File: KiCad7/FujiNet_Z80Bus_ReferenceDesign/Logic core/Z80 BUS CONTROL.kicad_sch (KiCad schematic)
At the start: 9 parts, among them IC6 7432N, IC7 7432N

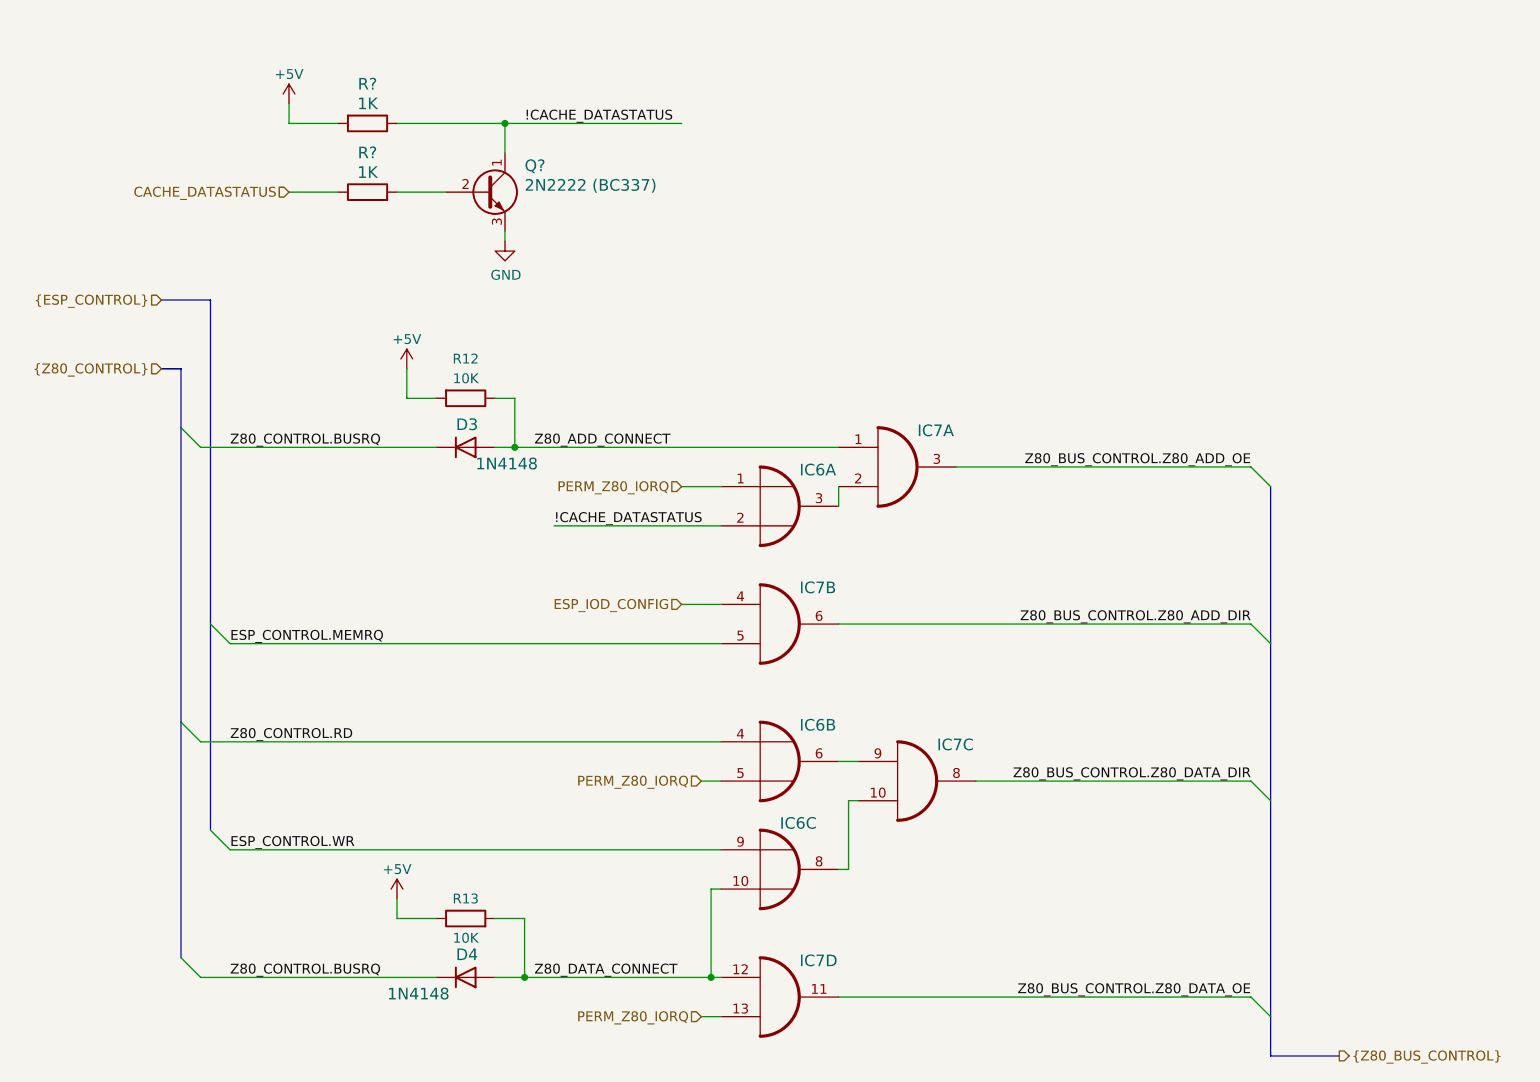
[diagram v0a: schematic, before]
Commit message: Unpicked CoreLogic Buses, some symbol updates
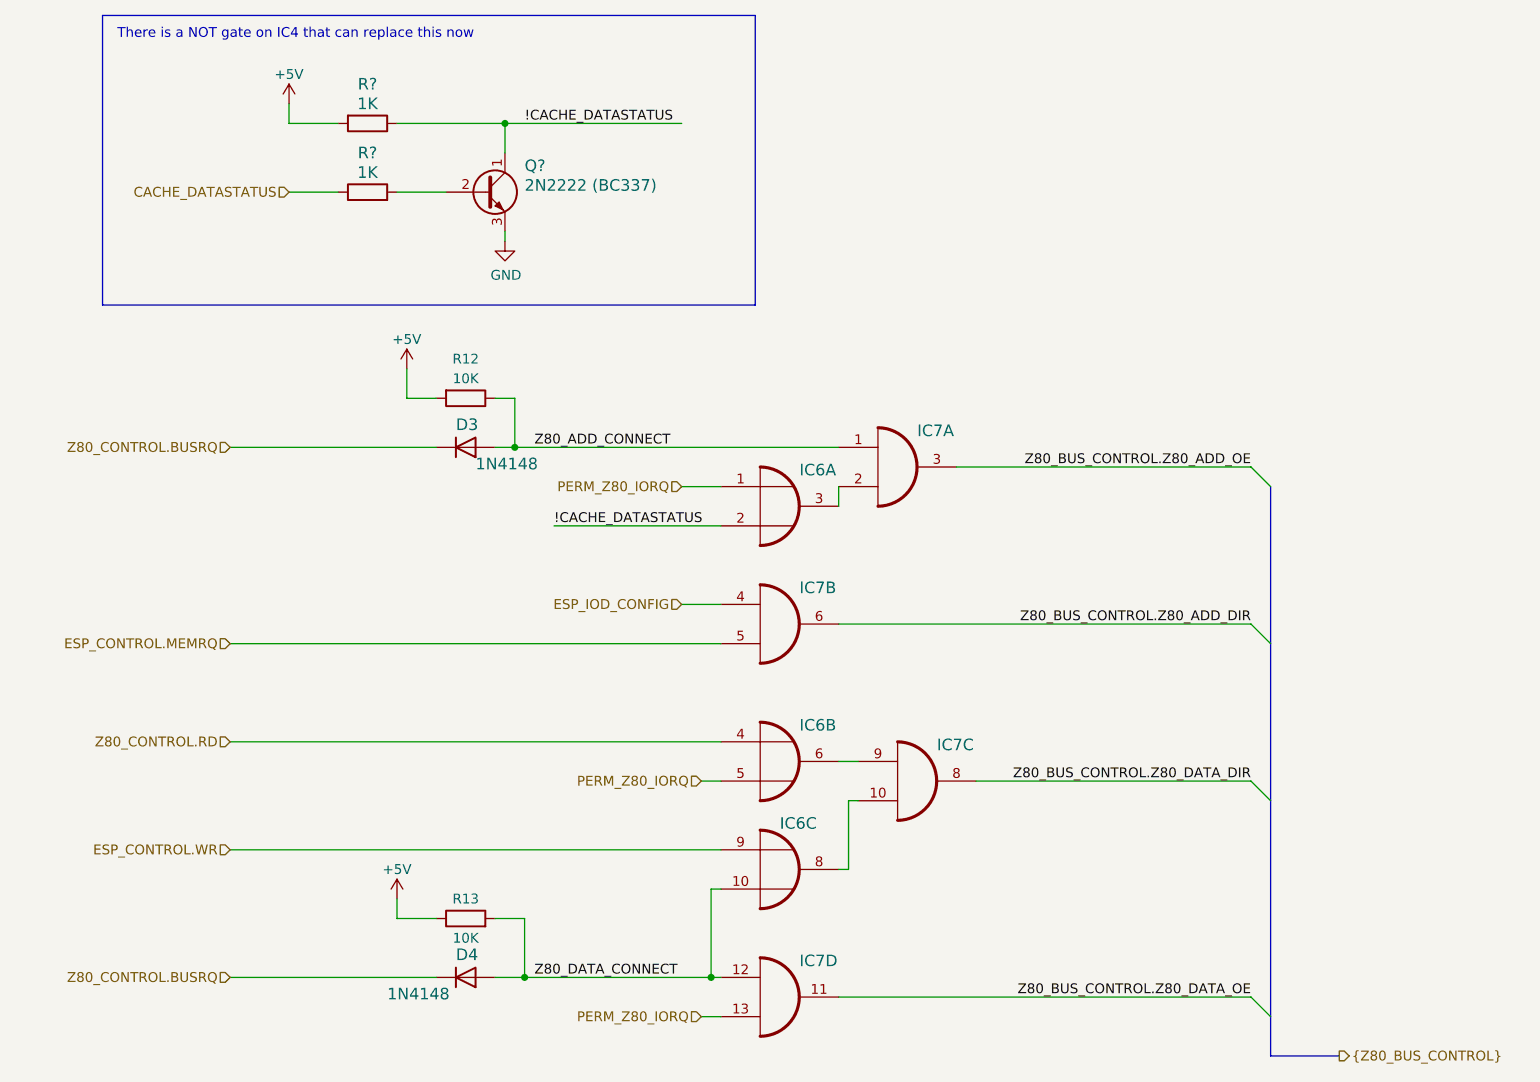
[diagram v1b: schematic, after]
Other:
- note added: "There is a NOT gate on IC4 that can replace this now"
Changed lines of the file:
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@@
-    (stroke (width 0) (type default))
-  )
-  (bus_entry (at 53.34 97.79) (size 2.54 2.54)
-    (stroke (width 0) (type default))
-  )
-  (bus_entry (at 49.53 140.97) (size 2.54 2.54)
     (stroke (width 0) (type default))
   )
@@
     (stroke (width 0) (type default))
   )
-  (bus_entry (at 52.07 74.93) (size -2.54 -2.54)
-    (stroke (width 0) (type default))
-  )
-  (bus_entry (at 49.53 110.49) (size 2.54 2.54)
-    (stroke (width 0) (type default))
-  )
-  (bus_entry (at 53.34 124.46) (size 2.54 2.54)
-    (stroke (width 0) (type default))
-  )
   (wire (pts (xy 91.44 33.02) (xy 91.44 36.83))
     (stroke (width 0) (type default))
@@
     (stroke (width 0) (type default))
   )
-  (bus (pts (xy 49.53 72.39) (xy 49.53 110.49))
-    (stroke (width 0) (type default))
-  )
   (wire (pts (xy 63.5 30.48) (xy 63.5 33.02))
     (stroke (width 0) (type default))
   )
-  (bus (pts (xy 46.99 64.77) (xy 49.53 64.77))
-    (stroke (width 0) (type default))
-  )
   (wire (pts (xy 119.38 80.01) (xy 114.3 80.01))
     (stroke (width 0) (type default))
@@
     (stroke (width 0) (type default))
   )
-  (bus (pts (xy 53.34 97.79) (xy 53.34 124.46))
-    (stroke (width 0) (type default))
-  )
   (wire (pts (xy 118.11 143.51) (xy 119.38 143.51))
     (stroke (width 0) (type default))
@@
     (stroke (width 0) (type default))
   )
-  (bus (pts (xy 46.99 55.88) (xy 53.34 55.88))
-    (stroke (width 0) (type default))
-  )
   (wire (pts (xy 63.5 33.02) (xy 69.85 33.02))
     (stroke (width 0) (type default))
@@
     (stroke (width 0) (type default))
   )
-  (wire (pts (xy 52.07 143.51) (xy 82.55 143.51))
-    (stroke (width 0) (type default))
-  )
   (wire (pts (xy 92.71 74.93) (xy 134.62 74.93))
     (stroke (width 0) (type default))
@@
     (stroke (width 0) (type default))
   )
-  (bus (pts (xy 49.53 110.49) (xy 49.53 140.97))
-    (stroke (width 0) (type default))
-  )
   (wire (pts (xy 118.11 132.08) (xy 119.38 132.08))
     (stroke (width 0) (type default))
@@
     (stroke (width 0) (type default))
   )
+  (wire (pts (xy 55.88 143.51) (xy 82.55 143.51))
+    (stroke (width 0) (type default))
+  )
   (wire (pts (xy 92.71 68.58) (xy 90.17 68.58))
     (stroke (width 0) (type default))
@@
     (stroke (width 0) (type default))
   )
-  (bus (pts (xy 49.53 64.77) (xy 49.53 72.39))
-    (stroke (width 0) (type default))
-  )
   (wire (pts (xy 116.84 118.11) (xy 119.38 118.11))
     (stroke (width 0) (type default))
@@
     (stroke (width 0) (type default))
   )
-  (bus (pts (xy 53.34 55.88) (xy 53.34 97.79))
-    (stroke (width 0) (type default))
-  )
-  (wire (pts (xy 52.07 113.03) (xy 119.38 113.03))
+  (wire (pts (xy 55.88 113.03) (xy 119.38 113.03))
     (stroke (width 0) (type default))
   )
@@
     (stroke (width 0) (type default))
   )
-  (wire (pts (xy 52.07 74.93) (xy 82.55 74.93))
+  (wire (pts (xy 55.88 74.93) (xy 82.55 74.93))
     (stroke (width 0) (type default))
   )
@@
     (stroke (width 0) (type default))
   )
-  (label "ESP_CONTROL.MEMRQ" (at 55.88 100.33 0) (fields_autoplaced)
+  (rectangle (start 39.37 19.05) (end 123.825 56.515)
+    (stroke (width 0) (type default))
+    (fill (type none))
+  )
+  (text "There is a NOT gate on IC4 that can replace this now"
+    (at 41.275 22.225 0)
     (effects (font (size 1.27 1.27)) (justify left bottom))
   )
@@
     (effects (font (size 1.27 1.27)) (justify right bottom))
   )
-  (label "Z80_CONTROL.RD" (at 55.88 113.03 0) (fields_autoplaced)
-    (effects (font (size 1.27 1.27)) (justify left bottom))
-  )
   (label "!CACHE_DATASTATUS" (at 93.98 33.02 0) (fields_autoplaced)
     (effects (font (size 1.27 1.27)) (justify left bottom))
@@
     (effects (font (size 1.27 1.27)) (justify left bottom))
   )
-  (label "Z80_CONTROL.BUSRQ" (at 55.88 143.51 0) (fields_autoplaced)
-    (effects (font (size 1.27 1.27)) (justify left bottom))
-  )
   (label "Z80_BUS_CONTROL.Z80_ADD_OE" (at 187.96 77.47 180) (fields_autoplaced)
     (effects (font (size 1.27 1.27)) (justify right bottom))
@@
     (effects (font (size 1.27 1.27)) (justify left bottom))
   )
-  (label "ESP_CONTROL.WR" (at 55.88 127 0) (fields_autoplaced)
-    (effects (font (size 1.27 1.27)) (justify left bottom))
-  )
-  (label "Z80_CONTROL.BUSRQ" (at 55.88 74.93 0) (fields_autoplaced)
-    (effects (font (size 1.27 1.27)) (justify left bottom))
-  )
   (hierarchical_label "PERM_Z80_IORQ" (shape input) (at 116.84 118.11 180) (fields_autoplaced)
     (effects (font (size 1.27 1.27)) (justify right))
@@
     (effects (font (size 1.27 1.27)) (justify right))
   )
-  (hierarchical_label "{ESP_CONTROL}" (shape input) (at 46.99 55.88 180) (fields_autoplaced)
+  (hierarchical_label "Z80_CONTROL.BUSRQ" (shape input) (at 55.88 74.93 180) (fields_autoplaced)
     (effects (font (size 1.27 1.27)) (justify right))
   )
@@
     (effects (font (size 1.27 1.27)) (justify left))
   )
+  (hierarchical_label "ESP_CONTROL.MEMRQ" (shape input) (at 55.88 100.33 180) (fields_autoplaced)
+    (effects (font (size 1.27 1.27)) (justify right))
+  )
   (hierarchical_label "PERM_Z80_IORQ" (shape input) (at 116.84 148.59 180) (fields_autoplaced)
     (effects (font (size 1.27 1.27)) (justify right))
   )
+  (hierarchical_label "Z80_CONTROL.BUSRQ" (shape input) (at 55.88 143.51 180) (fields_autoplaced)
+    (effects (font (size 1.27 1.27)) (justify right))
+  )
+  (hierarchical_label "Z80_CONTROL.RD" (shape input) (at 55.88 113.03 180) (fields_autoplaced)
+    (effects (font (size 1.27 1.27)) (justify right))
+  )
   (hierarchical_label "ESP_IOD_CONFIG" (shape input) (at 114.3 95.25 180) (fields_autoplaced)
     (effects (font (size 1.27 1.27)) (justify right))
@@
     (effects (font (size 1.27 1.27)) (justify right))
   )
-  (hierarchical_label "{Z80_CONTROL}" (shape input) (at 46.99 64.77 180) (fields_autoplaced)
+  (hierarchical_label "ESP_CONTROL.WR" (shape input) (at 55.88 127 180) (fields_autoplaced)
     (effects (font (size 1.27 1.27)) (justify right))
   )
@@
         )
         (path "/532c0392-800e-45cc-8170-6d32f2390e83/6a1fd481-1635-4a64-b244-c204161ad407/6bcd45ec-1810-4278-8058-96e26ec9b5f3"
-          (reference "IC6") (unit 3)
+          (reference "IC12") (unit 3)
         )
       )
@@
         )
         (path "/532c0392-800e-45cc-8170-6d32f2390e83/6a1fd481-1635-4a64-b244-c204161ad407/6bcd45ec-1810-4278-8058-96e26ec9b5f3"
-          (reference "#PWR027") (unit 1)
+          (reference "#PWR033") (unit 1)
         )
       )
@@
         )
         (path "/532c0392-800e-45cc-8170-6d32f2390e83/6a1fd481-1635-4a64-b244-c204161ad407/6bcd45ec-1810-4278-8058-96e26ec9b5f3"
-          (reference "IC6") (unit 2)
+          (reference "IC9") (unit 2)
         )
       )
@@
         )
         (path "/532c0392-800e-45cc-8170-6d32f2390e83/6a1fd481-1635-4a64-b244-c204161ad407/6bcd45ec-1810-4278-8058-96e26ec9b5f3"
-          (reference "IC6") (unit 1)
+          (reference "IC9") (unit 1)
         )
       )
@@
         )
         (path "/532c0392-800e-45cc-8170-6d32f2390e83/6a1fd481-1635-4a64-b244-c204161ad407/6bcd45ec-1810-4278-8058-96e26ec9b5f3"
-          (reference "D3") (unit 1)
+          (reference "D15") (unit 1)
         )
       )
@@
         )
         (path "/532c0392-800e-45cc-8170-6d32f2390e83/6a1fd481-1635-4a64-b244-c204161ad407/6bcd45ec-1810-4278-8058-96e26ec9b5f3"
-          (reference "IC7") (unit 4)
+          (reference "IC11") (unit 4)
         )
       )
@@
         )
         (path "/532c0392-800e-45cc-8170-6d32f2390e83/6a1fd481-1635-4a64-b244-c204161ad407/6bcd45ec-1810-4278-8058-96e26ec9b5f3"
-          (reference "R9") (unit 1)
+          (reference "R11") (unit 1)
         )
       )
@@
         )
         (path "/532c0392-800e-45cc-8170-6d32f2390e83/6a1fd481-1635-4a64-b244-c204161ad407/6bcd45ec-1810-4278-8058-96e26ec9b5f3"
-          (reference "R8") (unit 1)
+          (reference "R14") (unit 1)
         )
       )
@@
         )
         (path "/532c0392-800e-45cc-8170-6d32f2390e83/6a1fd481-1635-4a64-b244-c204161ad407/6bcd45ec-1810-4278-8058-96e26ec9b5f3"
-          (reference "IC7") (unit 3)
+          (reference "IC11") (unit 3)
         )
       )
@@
         )
         (path "/532c0392-800e-45cc-8170-6d32f2390e83/6a1fd481-1635-4a64-b244-c204161ad407/6bcd45ec-1810-4278-8058-96e26ec9b5f3"
-          (reference "IC7") (unit 1)
+          (reference "IC11") (unit 1)
         )
       )
@@
         )
         (path "/532c0392-800e-45cc-8170-6d32f2390e83/6a1fd481-1635-4a64-b244-c204161ad407/6bcd45ec-1810-4278-8058-96e26ec9b5f3"
-          (reference "#PWR034") (unit 1)
+          (reference "#PWR035") (unit 1)
         )
       )
@@
         )
         (path "/532c0392-800e-45cc-8170-6d32f2390e83/6a1fd481-1635-4a64-b244-c204161ad407/6bcd45ec-1810-4278-8058-96e26ec9b5f3"
-          (reference "IC7") (unit 2)
+          (reference "IC11") (unit 2)
         )
       )
@@
         )
         (path "/532c0392-800e-45cc-8170-6d32f2390e83/6a1fd481-1635-4a64-b244-c204161ad407/6bcd45ec-1810-4278-8058-96e26ec9b5f3"
-          (reference "D4") (unit 1)
+          (reference "D16") (unit 1)
         )
       )
@@
         )
         (path "/532c0392-800e-45cc-8170-6d32f2390e83/6a1fd481-1635-4a64-b244-c204161ad407/6bcd45ec-1810-4278-8058-96e26ec9b5f3"
-          (reference "#PWR033") (unit 1)
-        )
-      )
+          (reference "#PWR034") (unit 1)
+        )
+      )

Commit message: KiCad symbol library changes on logic core
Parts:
- IC6: value 7432N -> 74HC32N; symbol FujiNet_Z80Bus_Reference-rescue:7432N-Z80Decoder-eagle-import -> 74xx:74LS32
- IC7: value 7432N -> 74HC32N; symbol FujiNet_Z80Bus_Reference-rescue:7408N-Z80Decoder-eagle-import -> 74xx:74LS32
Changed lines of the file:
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@@
     )
   )
-  (symbol (lib_id "FujiNet_Z80Bus_Reference-rescue:7432N-Z80Decoder-eagle-import") (at 127 129.54 0) (unit 3)
+  (symbol (lib_id "74xx:74LS32") (at 127 129.54 0) (unit 3)
     (in_bom yes) (on_board yes) (dnp no)
     (property "Reference" "IC6" (at 127 124.46 0)
       (effects (font (size 1.4986 1.4986)) (justify left bottom))
     )
-    (property "Value" "7432N" (at 129.54 134.62 0)
+    (property "Value" "74HC32N" (at 129.54 134.62 0)
       (effects (font (size 1.4986 1.4986)) (justify left bottom) hide)
     )
@@
       (effects (font (size 1.27 1.27)) hide)
     )
-    (property "Datasheet" "" (at 127 129.54 0)
+    (property "Datasheet" "http://www.ti.com/lit/gpn/sn74LS32" (at 127 129.54 0)
       (effects (font (size 1.27 1.27)) hide)
     )
@@
     )
   )
-  (symbol (lib_id "FujiNet_Z80Bus_Reference-rescue:7432N-Z80Decoder-eagle-import") (at 127 115.57 0) (unit 2)
+  (symbol (lib_id "74xx:74LS32") (at 127 115.57 0) (unit 2)
     (in_bom yes) (on_board yes) (dnp no)
     (property "Reference" "IC6" (at 129.54 111.76 0)
       (effects (font (size 1.4986 1.4986)) (justify left bottom))
     )
-    (property "Value" "7432N" (at 129.54 120.65 0)
+    (property "Value" "74HC32N" (at 129.54 120.65 0)
       (effects (font (size 1.4986 1.4986)) (justify left bottom) hide)
     )
@@
       (effects (font (size 1.27 1.27)) hide)
     )
-    (property "Datasheet" "" (at 127 115.57 0)
+    (property "Datasheet" "http://www.ti.com/lit/gpn/sn74LS32" (at 127 115.57 0)
       (effects (font (size 1.27 1.27)) hide)
     )
@@
     )
   )
-  (symbol (lib_id "FujiNet_Z80Bus_Reference-rescue:7432N-Z80Decoder-eagle-import") (at 127 82.55 0) (unit 1)
+  (symbol (lib_id "74xx:74LS32") (at 127 82.55 0) (unit 1)
     (in_bom yes) (on_board yes) (dnp no)
     (property "Reference" "IC6" (at 129.54 78.74 0)
       (effects (font (size 1.4986 1.4986)) (justify left bottom))
     )
-    (property "Value" "7432N" (at 129.54 87.63 0)
+    (property "Value" "74HC32N" (at 129.54 87.63 0)
       (effects (font (size 1.4986 1.4986)) (justify left bottom) hide)
     )
@@
       (effects (font (size 1.27 1.27)) hide)
     )
-    (property "Datasheet" "" (at 127 82.55 0)
+    (property "Datasheet" "http://www.ti.com/lit/gpn/sn74LS32" (at 127 82.55 0)
       (effects (font (size 1.27 1.27)) hide)
     )
@@
     )
   )
-  (symbol (lib_id "FujiNet_Z80Bus_Reference-rescue:7408N-Z80Decoder-eagle-import") (at 127 146.05 0) (unit 4)
+  (symbol (lib_id "74xx:74LS32") (at 127 146.05 0) (unit 4)
     (in_bom yes) (on_board yes) (dnp no)
     (property "Reference" "IC7" (at 129.54 142.24 0)
       (effects (font (size 1.4986 1.4986)) (justify left bottom))
     )
-    (property "Value" "7432N" (at 129.54 151.13 0)
+    (property "Value" "74HC32N" (at 129.54 151.13 0)
       (effects (font (size 1.4986 1.4986)) (justify left bottom) hide)
     )
@@
       (effects (font (size 1.27 1.27)) hide)
     )
-    (property "Datasheet" "" (at 127 146.05 0)
+    (property "Datasheet" "http://www.ti.com/lit/gpn/sn74LS32" (at 127 146.05 0)
       (effects (font (size 1.27 1.27)) hide)
     )
@@
     )
   )
-  (symbol (lib_id "FujiNet_Z80Bus_Reference-rescue:7408N-Z80Decoder-eagle-import") (at 144.78 118.11 0) (unit 3)
+  (symbol (lib_id "74xx:74LS32") (at 144.78 118.11 0) (unit 3)
     (in_bom yes) (on_board yes) (dnp no)
     (property "Reference" "IC7" (at 147.32 114.3 0)
       (effects (font (size 1.4986 1.4986)) (justify left bottom))
     )
-    (property "Value" "7432N" (at 147.32 123.19 0)
+    (property "Value" "74HC32N" (at 147.32 123.19 0)
       (effects (font (size 1.4986 1.4986)) (justify left bottom) hide)
     )
@@
       (effects (font (size 1.27 1.27)) hide)
     )
-    (property "Datasheet" "" (at 144.78 118.11 0)
+    (property "Datasheet" "http://www.ti.com/lit/gpn/sn74LS32" (at 144.78 118.11 0)
       (effects (font (size 1.27 1.27)) hide)
     )
@@
     )
   )
-  (symbol (lib_id "FujiNet_Z80Bus_Reference-rescue:7408N-Z80Decoder-eagle-import") (at 142.24 77.47 0) (unit 1)
+  (symbol (lib_id "74xx:74LS32") (at 142.24 77.47 0) (unit 1)
     (in_bom yes) (on_board yes) (dnp no)
     (property "Reference" "IC7" (at 144.78 73.66 0)
       (effects (font (size 1.4986 1.4986)) (justify left bottom))
     )
-    (property "Value" "7432N" (at 144.78 82.55 0)
+    (property "Value" "74HC32N" (at 144.78 82.55 0)
       (effects (font (size 1.4986 1.4986)) (justify left bottom) hide)
     )
@@
       (effects (font (size 1.27 1.27)) hide)
     )
-    (property "Datasheet" "" (at 142.24 77.47 0)
+    (property "Datasheet" "http://www.ti.com/lit/gpn/sn74LS32" (at 142.24 77.47 0)
       (effects (font (size 1.27 1.27)) hide)
     )
@@
     )
   )
-  (symbol (lib_id "FujiNet_Z80Bus_Reference-rescue:7408N-Z80Decoder-eagle-import") (at 127 97.79 0) (unit 2)
+  (symbol (lib_id "74xx:74LS32") (at 127 97.79 0) (unit 2)
     (in_bom yes) (on_board yes) (dnp no)
     (property "Reference" "IC7" (at 129.54 93.98 0)
       (effects (font (size 1.4986 1.4986)) (justify left bottom))
     )
-    (property "Value" "7432N" (at 129.54 102.87 0)
+    (property "Value" "74HC32N" (at 129.54 102.87 0)
       (effects (font (size 1.4986 1.4986)) (justify left bottom) hide)
     )
@@
       (effects (font (size 1.27 1.27)) hide)
     )
-    (property "Datasheet" "" (at 127 97.79 0)
-      (effects (font (size 1.27 1.27)) hide)
-    )
+    (property "Datasheet" "http://www.ti.com/lit/gpn/sn74LS32" (at 127 97.79 0)
+      (effects (font (size 1.27 1.27)) hide)
+    )

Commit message: Kicad Symbols error fixes and ERC bug fixes
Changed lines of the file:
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@@
       (effects (font (size 1.4986 1.4986)) (justify left bottom))
     )
-    (property "Value" "1N4148" (at 87.63 76.2 0)
+    (property "Value" "1N4148" (at 83.82 77.47 0)
       (effects (font (size 1.4986 1.4986)) (justify left bottom))
     )
@@
       (effects (font (size 1.4986 1.4986)) (justify left bottom))
     )
-    (property "Value" "1N4148" (at 76.2 144.78 0)
-      (effects (font (size 1.4986 1.4986)) (justify left bottom))
-    )
+    (property "Value" "1N4148" (at 82.55 146.05 0)
+      (effects (font (size 1.4986 1.4986)) (justify left bottom))
+    )
